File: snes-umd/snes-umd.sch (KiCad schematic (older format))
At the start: 1 part

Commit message: sch work on SNES adapter
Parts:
- added C102: SNES-CONN, db-thparts:SNES-CONN-EXP, symbol SNES-CONN
- C101: footprint (none) -> db-thparts:UMD-CONN-DIP64
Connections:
- net labels added: +5V, A0, A1, A10, A11, A12, A13, A14, A15, A16, A17, A18, A19, A2, A20, A21, A22, A23, A3, A4, A5, A6, A7, A8, A9, D0, D1, D12, D13, D14, D15, D2, D3, D4, D5, D6, D7, GND, ~CE, ~RD, ~RESET, ~WR
- wire segments 0 -> 74
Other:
- moved on the sheet: C101A, C101B

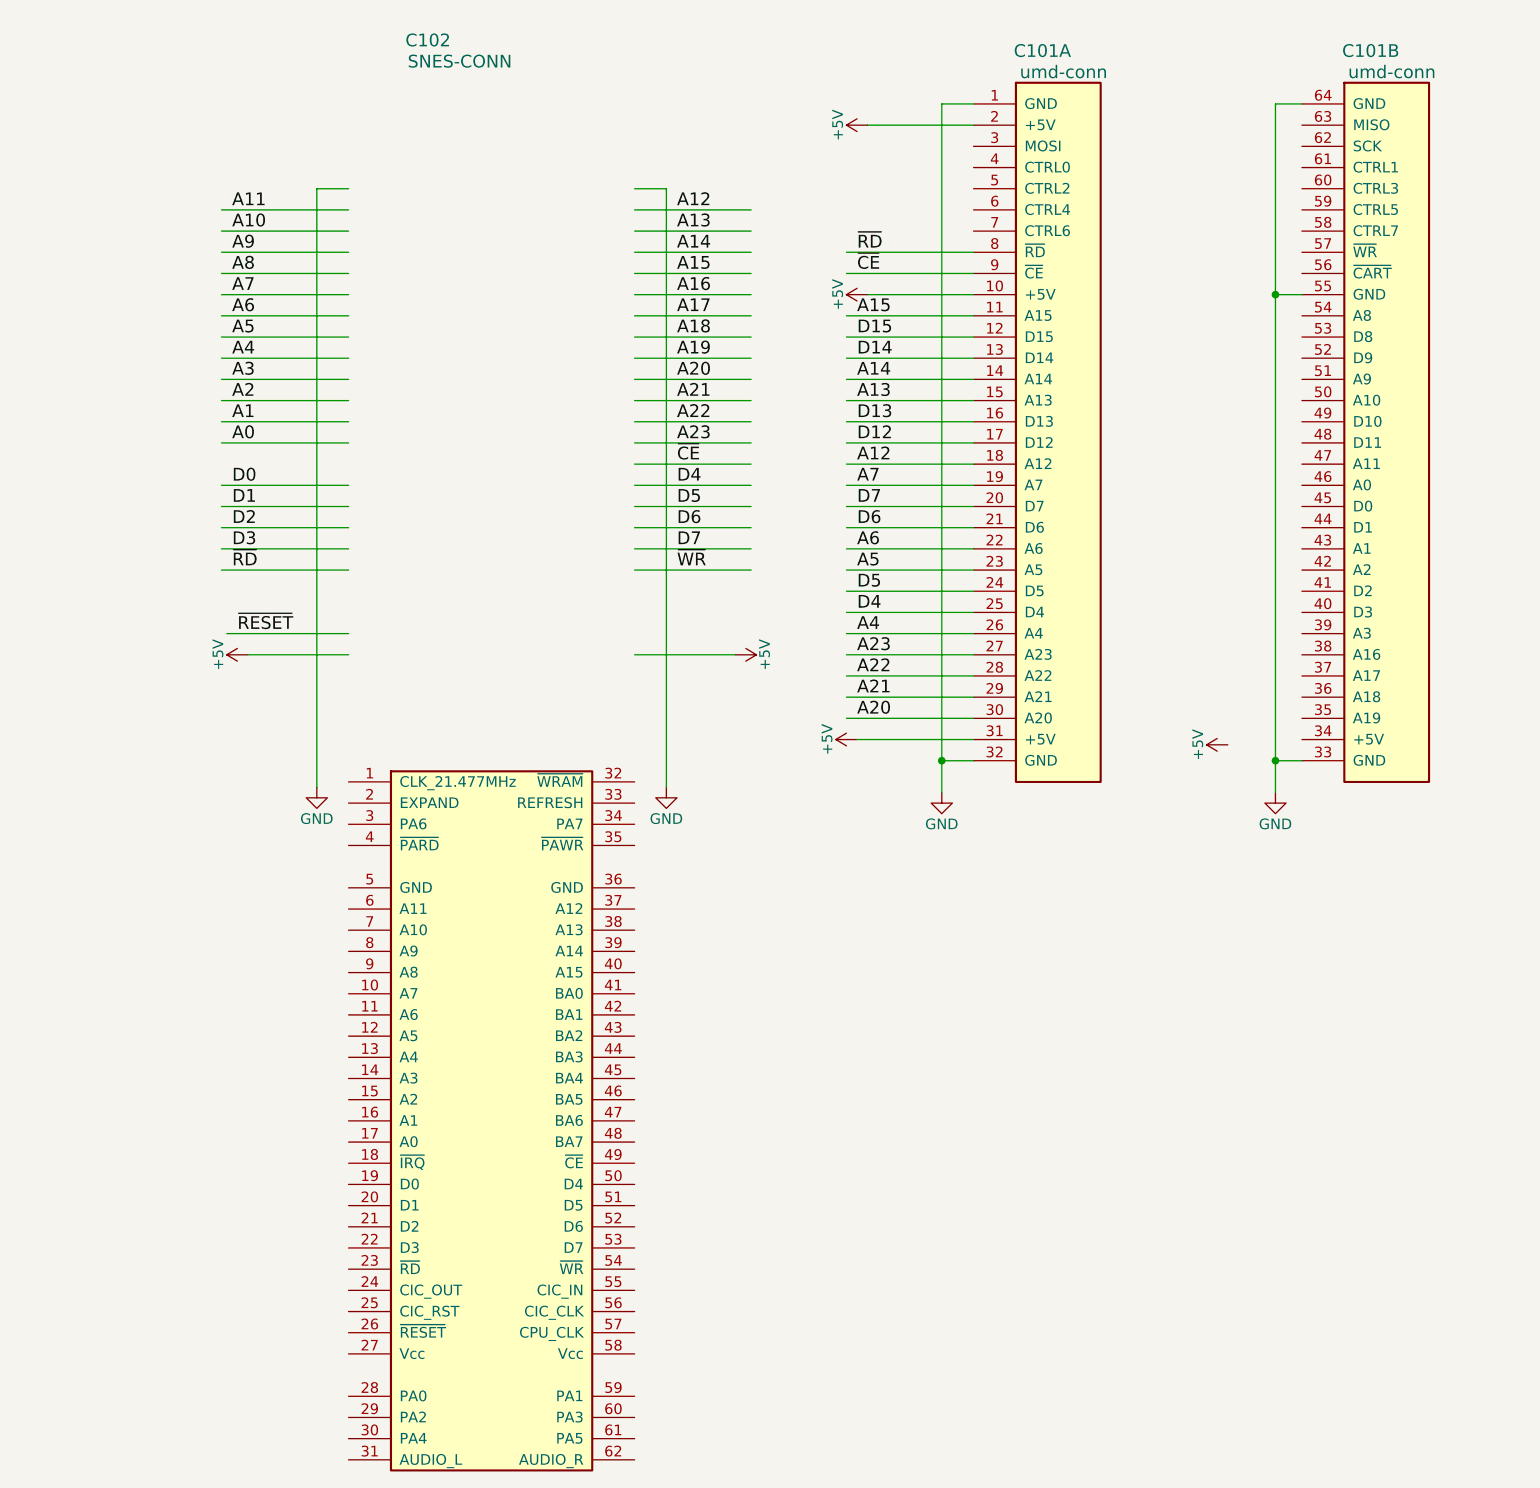
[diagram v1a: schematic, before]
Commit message: finished schematic, board outline complete
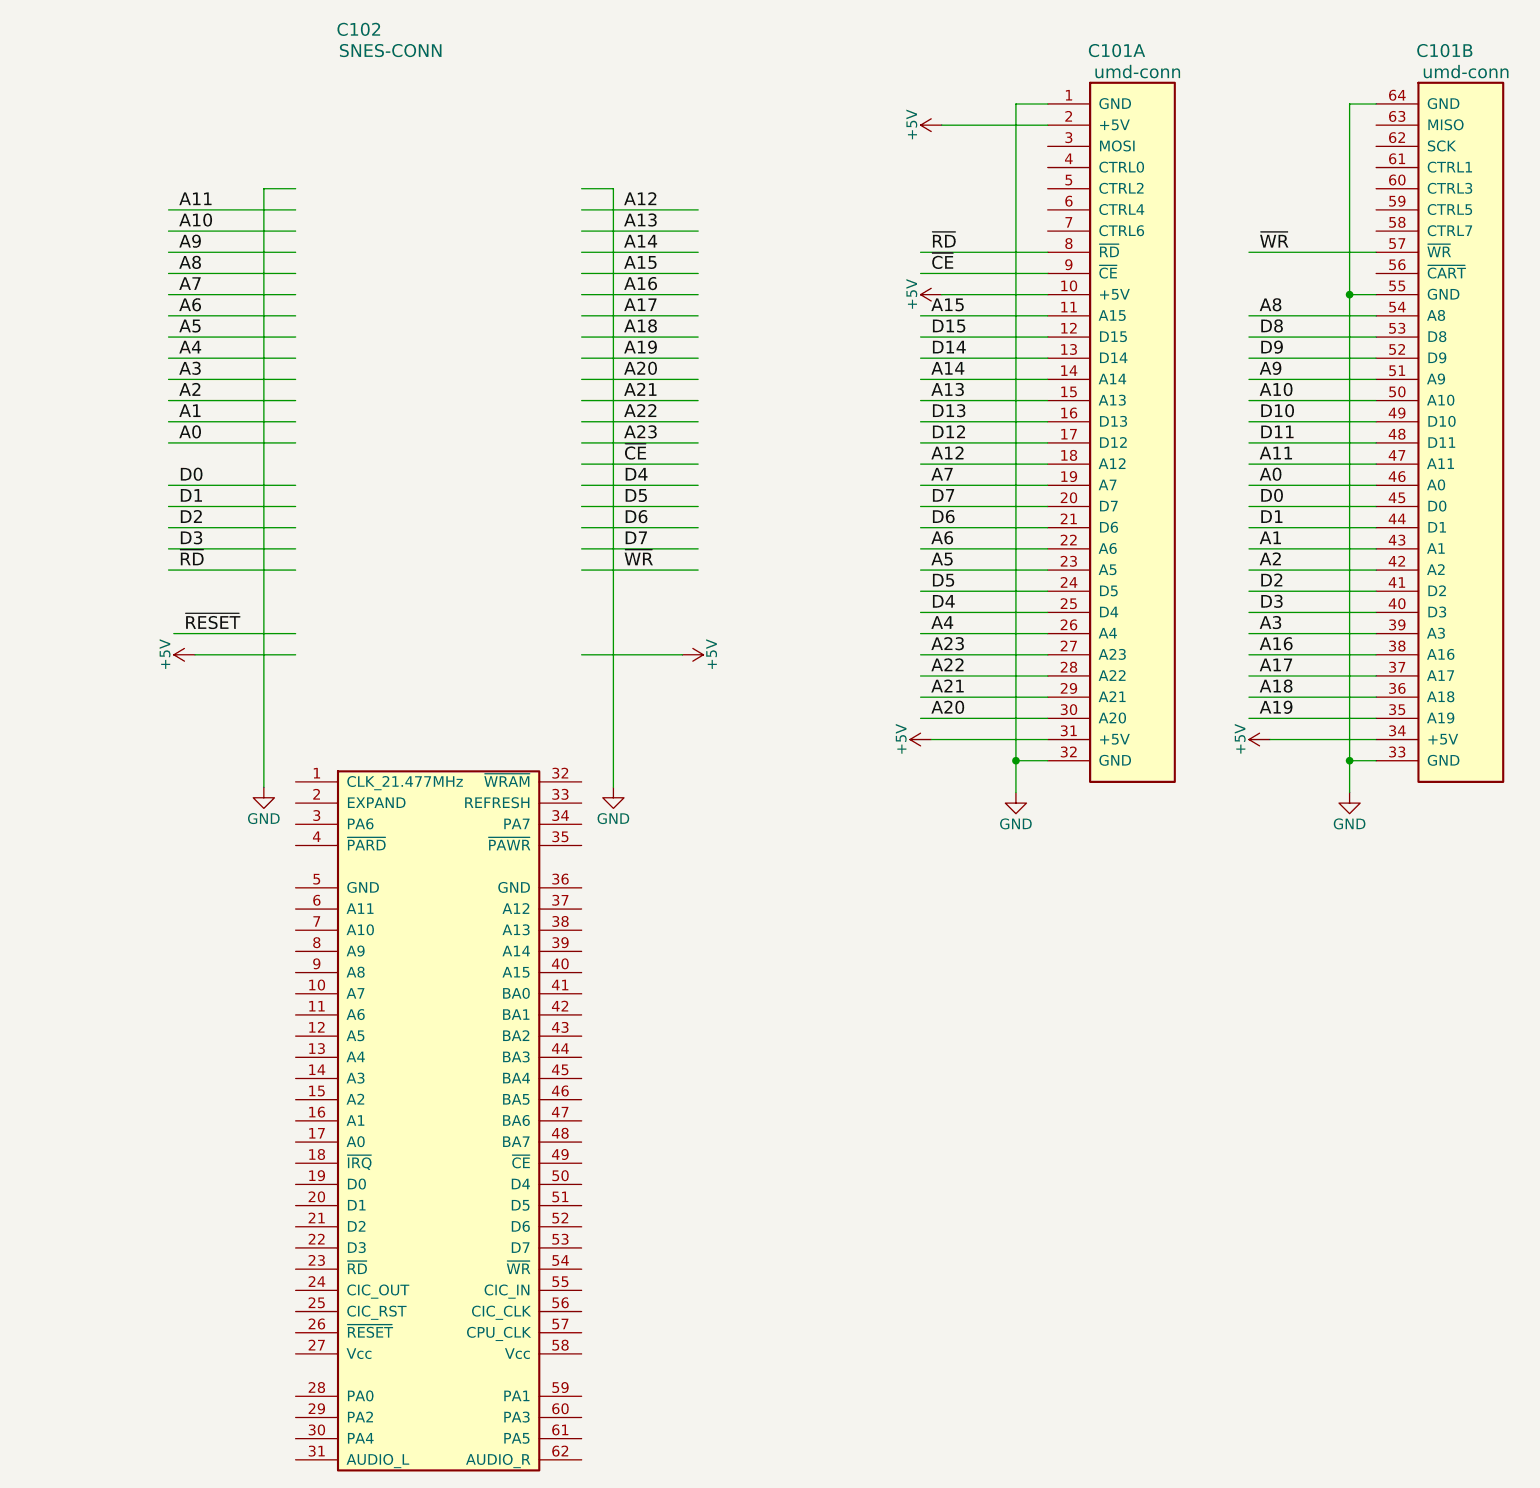
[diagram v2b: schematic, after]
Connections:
- net labels added: D10, D11, D8, D9
- wire segments 74 -> 96
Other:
- moved on the sheet: C101A, C101B

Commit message: routing the pcb, learning KiCad
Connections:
- wire segments 96 -> 91
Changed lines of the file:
@@
 L GND #PWR04
 U 1 1 5A60BBAB
-P 8375 5600
-F 0 "#PWR04" H 8375 5350 50  0001 C CNN
-F 1 "GND" H 8375 5450 50  0000 C CNN
-F 2 "" H 8375 5600 50  0001 C CNN
-F 3 "" H 8375 5600 50  0001 C CNN
-	1    8375 5600
+P 8350 5600
+F 0 "#PWR04" H 8350 5350 50  0001 C CNN
+F 1 "GND" H 8350 5450 50  0000 C CNN
+F 2 "" H 8350 5600 50  0001 C CNN
+F 3 "" H 8350 5600 50  0001 C CNN
+	1    8350 5600
 	1    0    0    -1
 $EndComp
@@
 Wire Wire Line
 	4900 2750 4900 5575
-Wire Wire Line
-	6950 5450 6800 5450
-Wire Wire Line
-	6800 2350 6800 5600
-Wire Wire Line
-	6950 2350 6800 2350
-Connection ~ 6800 5450
-Wire Wire Line
-	8375 5450 8500 5450
-Wire Wire Line
-	8375 2350 8375 5600
-Wire Wire Line
-	8500 3250 8375 3250
-Connection ~ 8375 5450
-Wire Wire Line
-	8500 2350 8375 2350
-Connection ~ 8375 3250
 Wire Wire Line
 	3400 4550 2800 4550
@@
 Wire Wire Line
 	6450 2450 6950 2450
-$Comp
-L +5V #PWR08
-U 1 1 5A61057C
-P 6400 5350
-F 0 "#PWR08" H 6400 5200 50  0001 C CNN
-F 1 "+5V" H 6400 5490 50  0000 C CNN
-F 2 "" H 6400 5350 50  0001 C CNN
-F 3 "" H 6400 5350 50  0001 C CNN
-	1    6400 5350
-	0    -1   -1   0
-$EndComp
-$Comp
-L +5V #PWR010
-U 1 1 5A6105A4
-P 6450 3250
-F 0 "#PWR010" H 6450 3100 50  0001 C CNN
-F 1 "+5V" H 6450 3390 50  0000 C CNN
-F 2 "" H 6450 3250 50  0001 C CNN
-F 3 "" H 6450 3250 50  0001 C CNN
-	1    6450 3250
-	0    -1   -1   0
-$EndComp
-Wire Wire Line
-	6950 3250 6450 3250
-Wire Wire Line
-	6400 5350 6950 5350
 Wire Wire Line
 	6950 3550 6350 3550
@@
 Text Label 7950 5250 0    60   ~ 0
 A19
-$Comp
-L +5V #PWR?
-U 1 1 5A62004C
-P 8000 5350
-F 0 "#PWR?" H 8000 5200 50  0001 C CNN
-F 1 "+5V" H 8000 5490 50  0000 C CNN
-F 2 "" H 8000 5350 50  0001 C CNN
-F 3 "" H 8000 5350 50  0001 C CNN
-	1    8000 5350
-	0    -1   -1   0
-$EndComp
-Wire Wire Line
-	8500 5350 8000 5350
 Wire Wire Line
 	8500 3050 7900 3050
@@
 	1    0    0    -1
 $EndComp
+Wire Wire Line
+	8500 2950 7900 2950
+Text Label 7950 2950 0    60   ~ 0
+~RESET
+Wire Wire Line
+	6950 5450 6800 5450
+Wire Wire Line
+	6800 5450 6800 5600
+Wire Wire Line
+	8500 5450 8350 5450
+Wire Wire Line
+	8350 5450 8350 5600
 $EndSCHEMATC

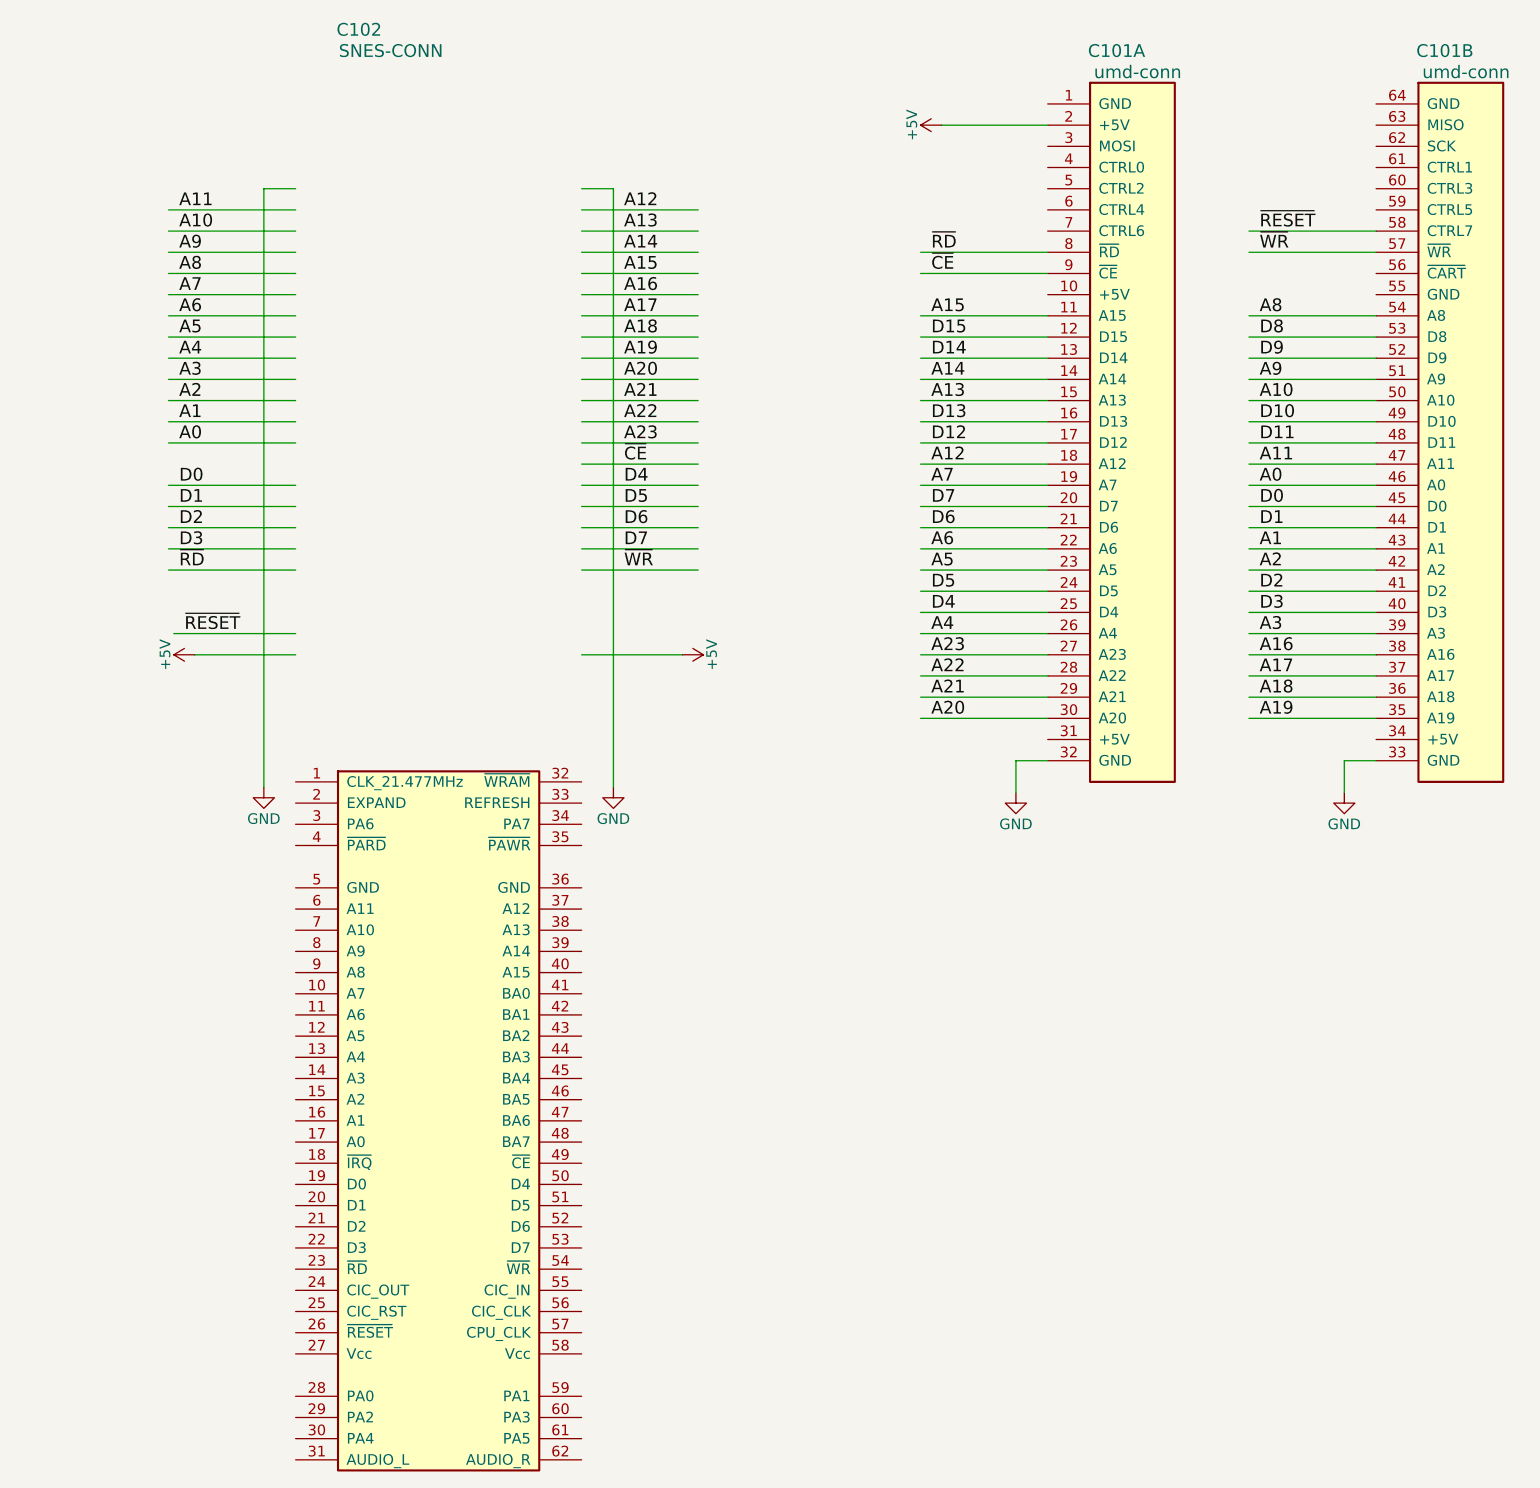
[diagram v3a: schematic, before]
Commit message: PCB routing verification finished, adjusted date code
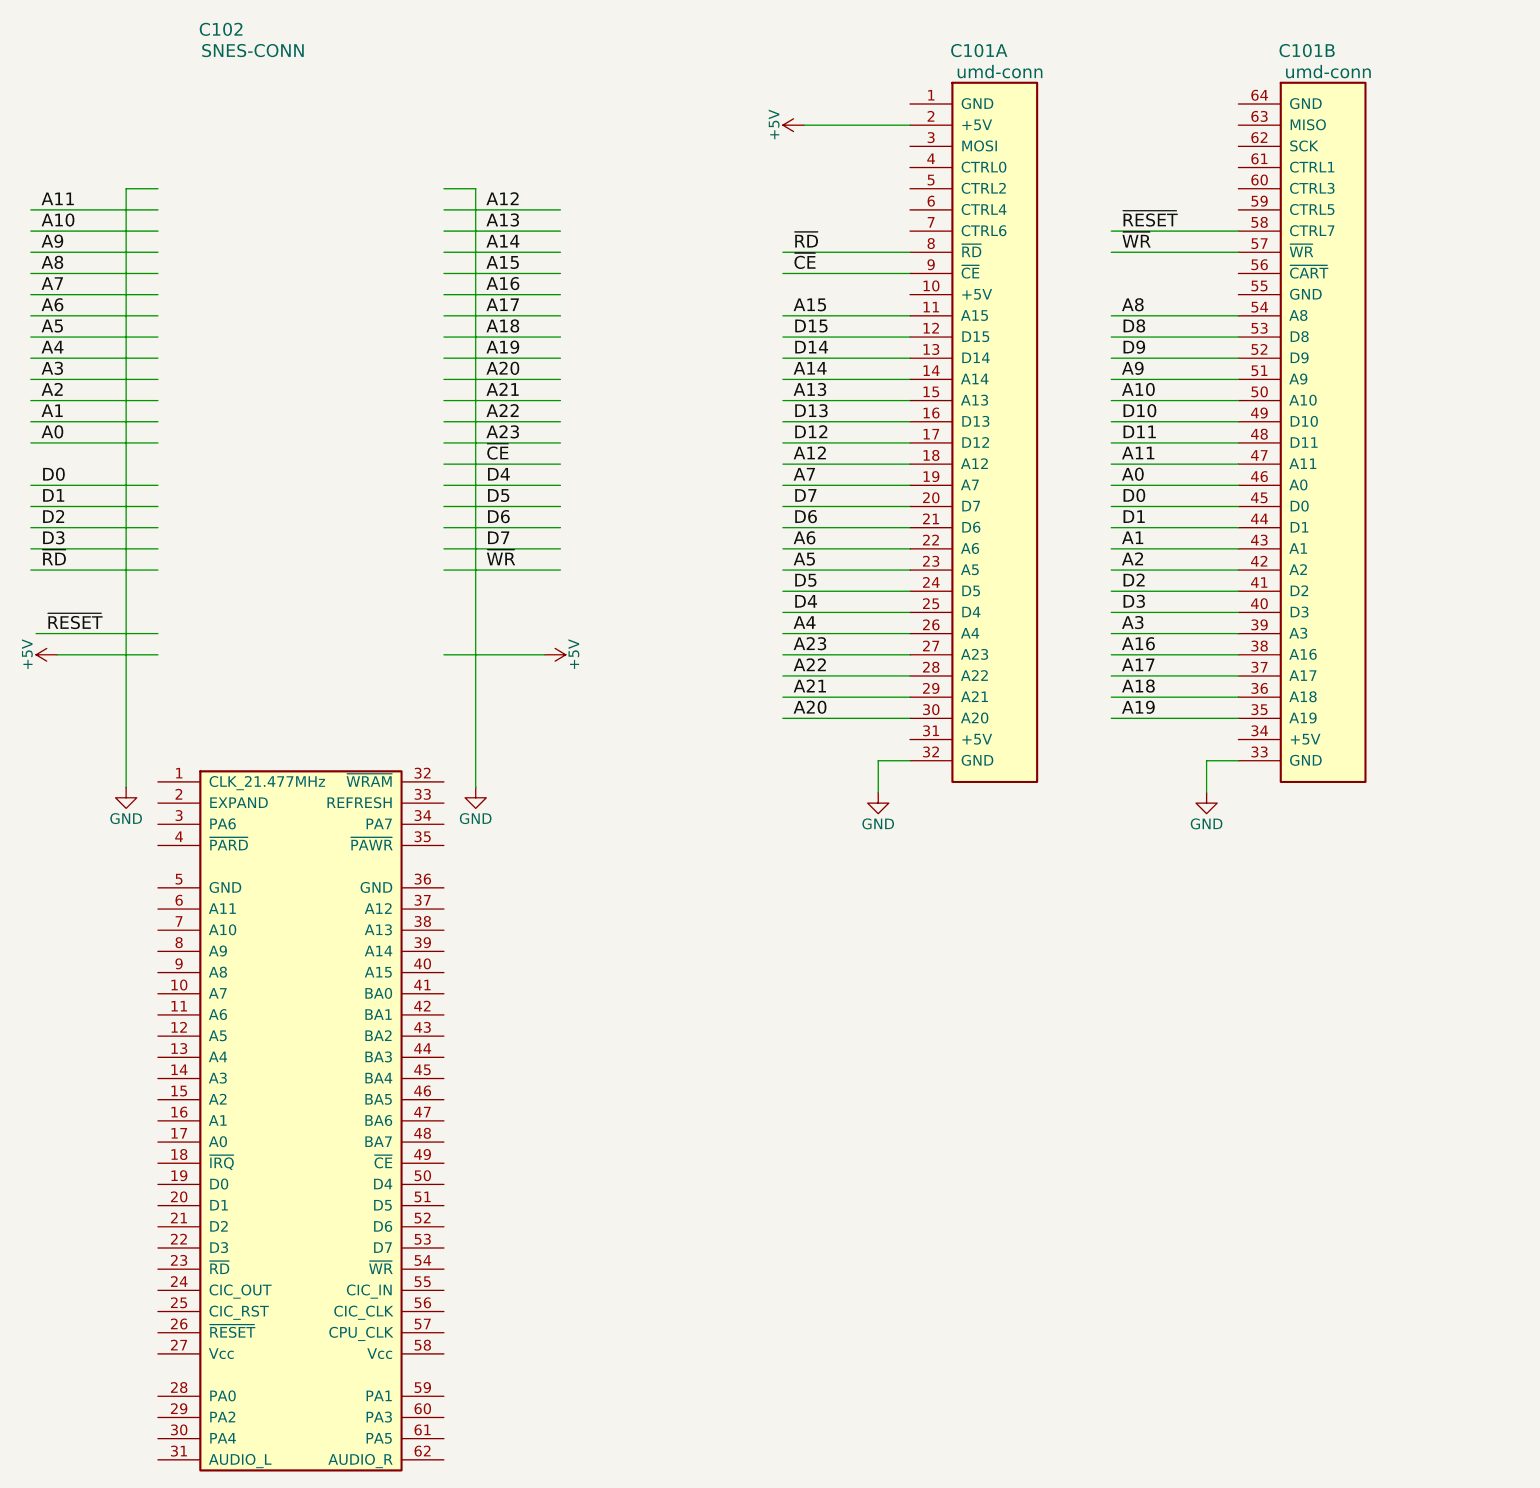
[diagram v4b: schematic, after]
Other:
- moved on the sheet: C101A, C101B, C102

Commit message: new NES UMD adapter PCB
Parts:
- C102: symbol SNES-CONN -> SNES-CONN-RESCUE-snes-umd
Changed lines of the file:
@@
 EESchema Schematic File Version 2
+LIBS:snes-umd-rescue
 LIBS:db-diodes
 LIBS:db-memory
@@
 ~WR
 $Comp
-L SNES-CONN C102
+L SNES-CONN-RESCUE-snes-umd C102
 U 1 1 5A62100A
 P 2950 5500
